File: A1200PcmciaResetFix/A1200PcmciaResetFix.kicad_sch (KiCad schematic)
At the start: 7 parts, among them J1 ADDR, J2 RESET, Q1 BC807, U1 ACT1225PL84

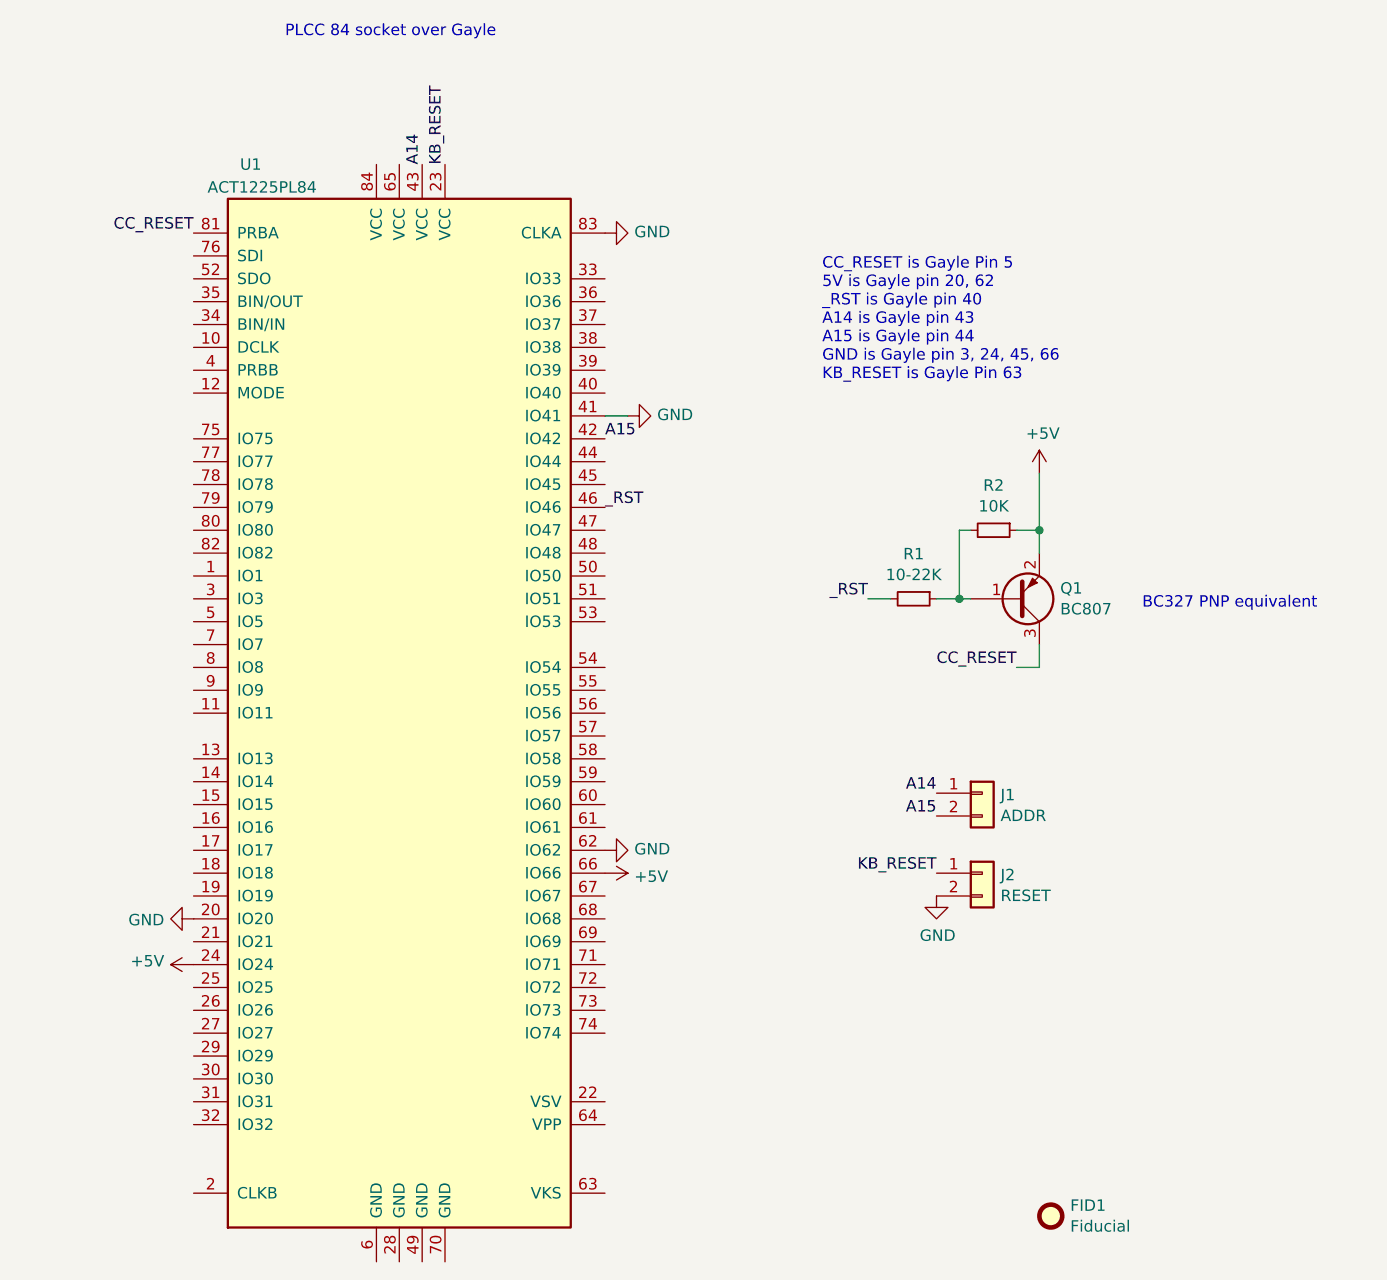
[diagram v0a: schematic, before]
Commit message: A1200PcmciaResetFix, A600-1200KeyboardSocket : update socket symbol and footprint, no PCB change
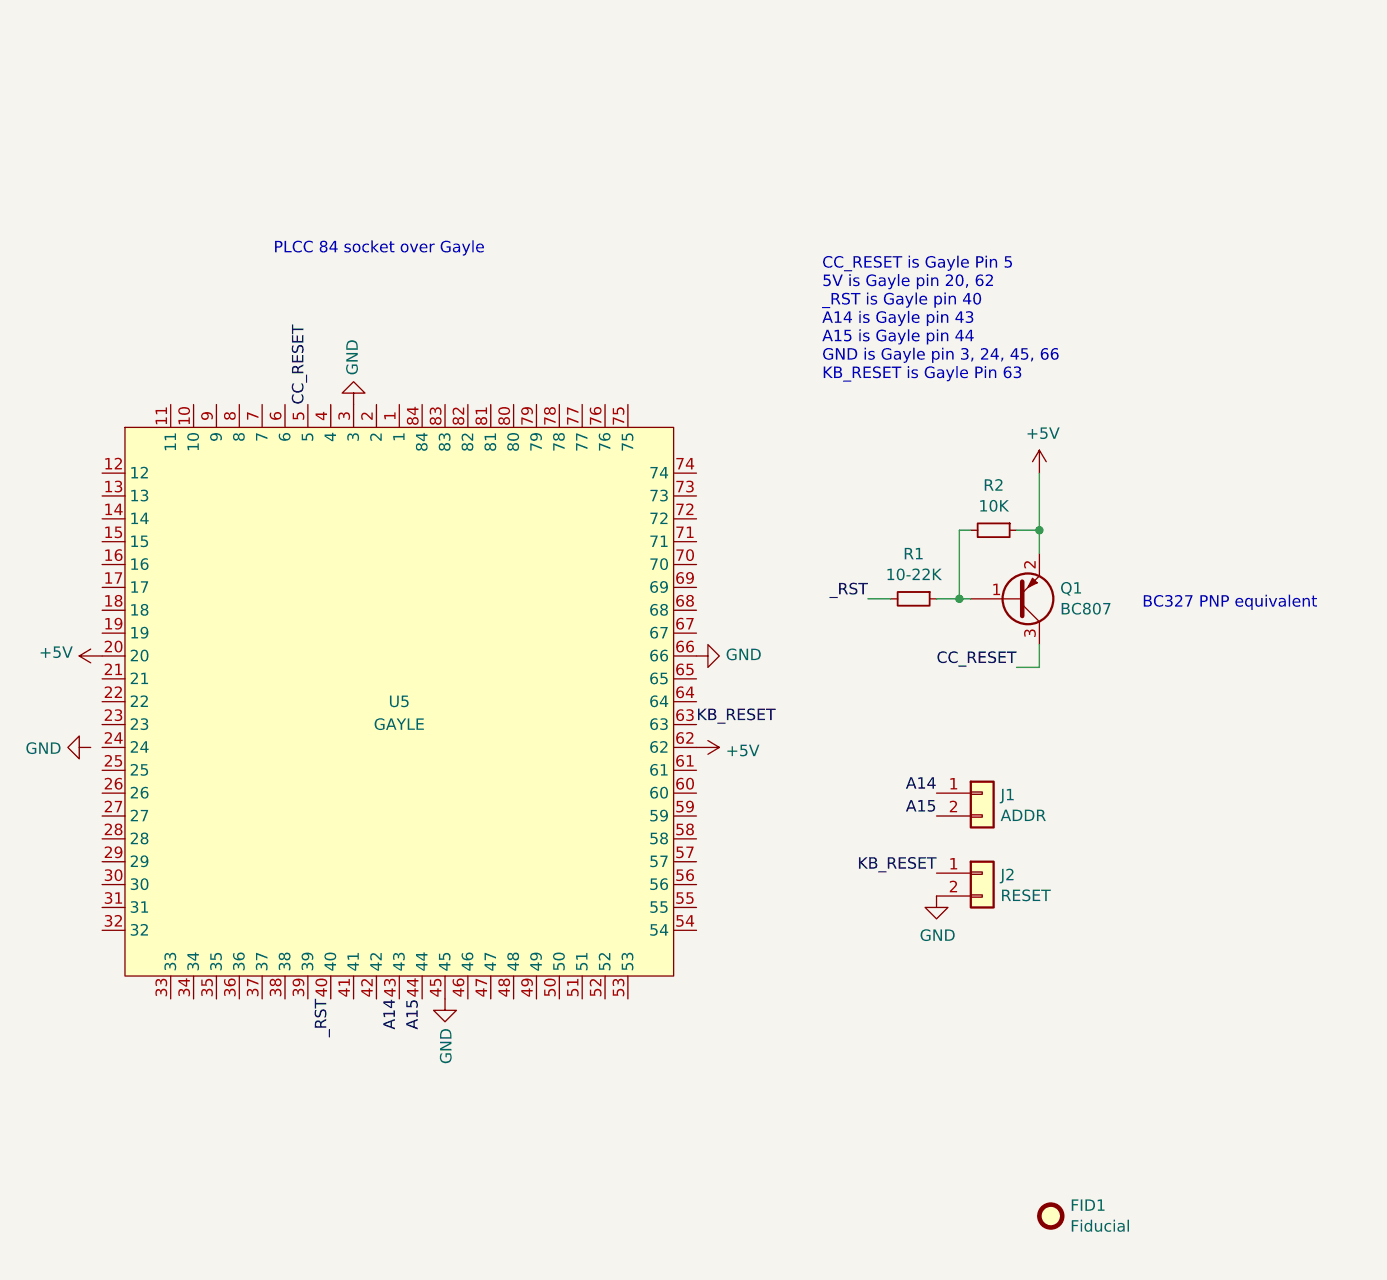
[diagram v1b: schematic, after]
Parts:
- removed U1: ACT1225PL84, Package_LCC:PLCC-84_THT-Socket, symbol FPGA_Microsemi:ACT1225PL84
- added U5: GAYLE, Sassa:PLCC-84_THT-SocketOnTop, symbol Sassa:PLCC-84
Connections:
- net +5V: now also U5.20, U5.62
- net A14: now also U5.43
- net A15: now also U5.44
- net CC_RESET: now also U5.5
- net GND: now also U5.3, U5.45, U5.66
- net KB_RESET: now also U5.63
- net _RST: now also U5.40
